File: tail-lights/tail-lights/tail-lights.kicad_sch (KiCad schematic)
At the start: 106 parts, among them IC1 ATMEGA328P-AU, IC2 NCV8402ASTT1G, IC3 NCV8402ASTT1G, IC4 NCV8402ASTT1G, IC5 TPS62160DGKR, J1 Conn_01x01, J2 Conn_01x01, J3 Conn_01x06_Female, J4 Conn_01x04_Female, Y1 X322516MLB4SI

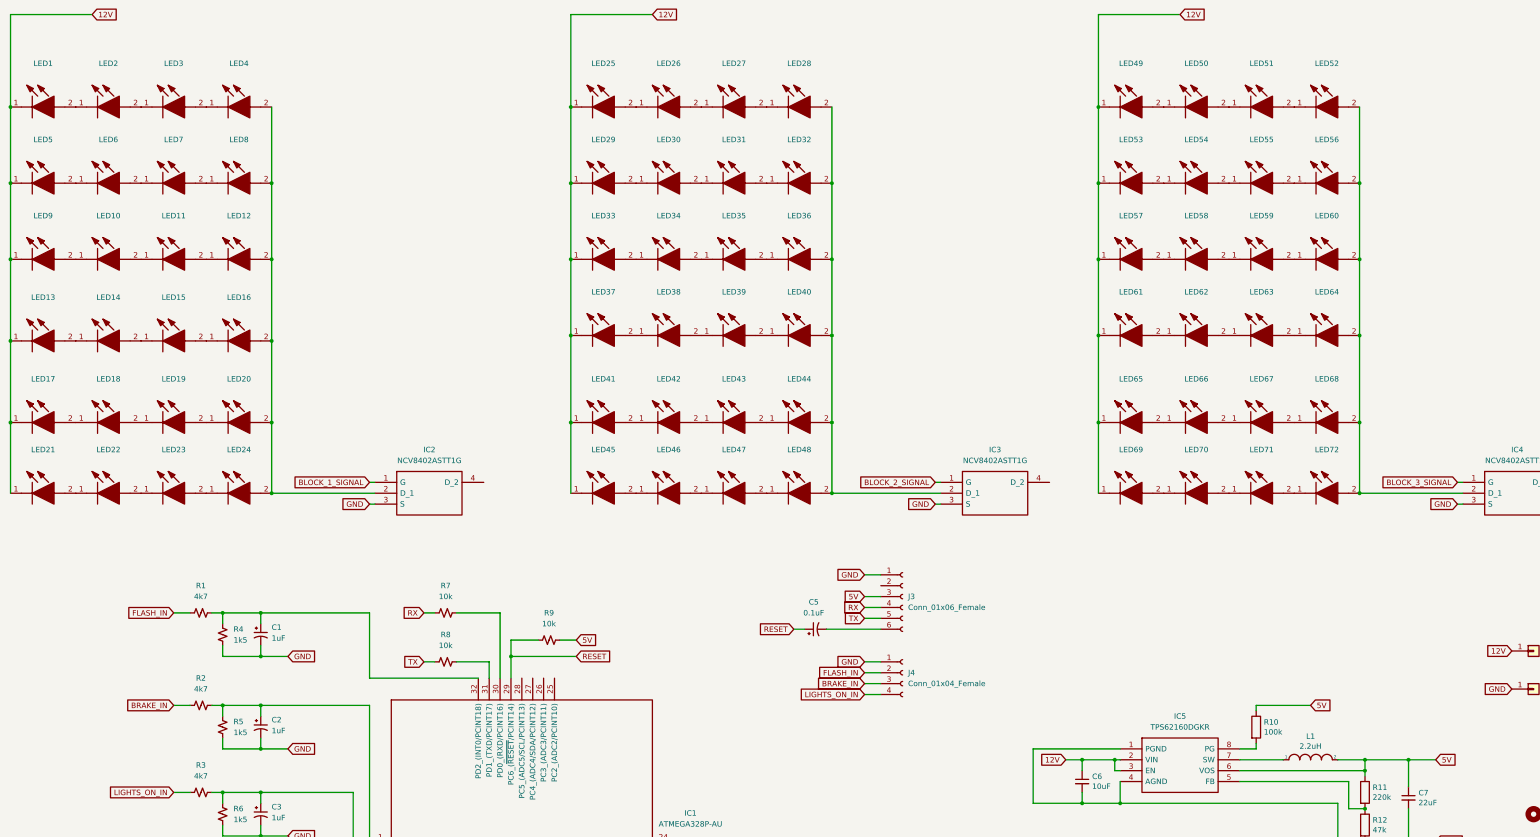
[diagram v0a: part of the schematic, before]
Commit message: Finalise tail-lights. Send off for fab
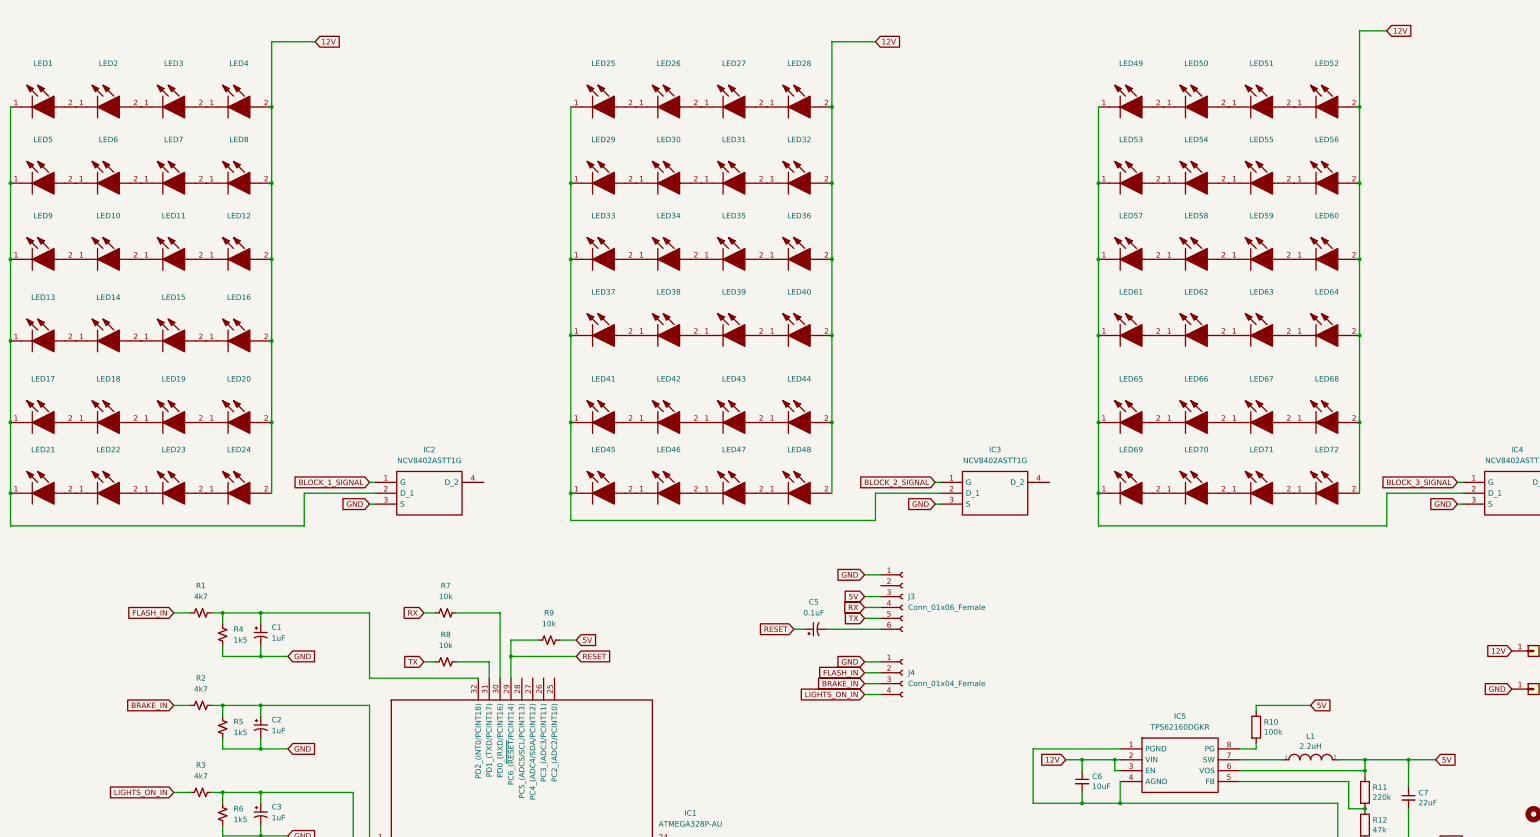
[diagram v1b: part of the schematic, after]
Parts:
- L1: footprint Inductor_SMD:NR6028T220M -> Library:NR6028T220M
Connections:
- net 12V: now also LED12.2, LED16.2, LED20.2, LED24.2, LED28.2, LED32.2, LED36.2, LED4.2, LED40.2, LED44.2, LED48.2, LED52.2, LED56.2, LED60.2, LED64.2, LED68.2, LED72.2, LED8.2; no longer LED1.1, LED13.1, LED17.1, LED21.1, LED25.1, LED29.1, LED33.1, LED37.1, LED41.1, LED45.1, LED49.1, LED5.1, LED53.1, LED57.1, LED61.1, LED65.1, LED69.1, LED9.1
- new net: IC2.2 (D_1), LED1.1, LED13.1, LED17.1, LED21.1, LED5.1, LED9.1
- new net: IC4.2 (D_1), LED49.1, LED53.1, LED57.1, LED61.1, LED65.1, LED69.1
- new net: IC3.2 (D_1), LED25.1, LED29.1, LED33.1, LED37.1, LED41.1, LED45.1

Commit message: Send tail lights v2 for fabrication
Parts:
- removed H1, H2, H3, H4: MountingHole, MountingHole:MountingHole_2.5mm_Pad, symbol Mechanical:MountingHole
- added C8: 0.1uF, Capacitor_SMD:C_0603_1608Metric, symbol Device:C_Polarized_Small_US
- added H1, H2, H3, H5: MountingHole_Pad, MountingHole:MountingHole_2.5mm_Pad, symbol Mechanical:MountingHole_Pad
- added IC6, IC7, IC8: L7812CV, Library:TO255P460X1020X2008-3P, symbol Power_Protection:L7812CV
- added J10, J11, J12, J13, J14, J15, J16, J6, J7, J8, J9: Conn_01x01_Pin, Connector_PinHeader_2.54mm:PinHeader_1x01_P2.54mm_Vertical, symbol Connector:Conn_01x01_Pin
- added J5: Conn_01x06_Female, Connector_PinHeader_2.54mm:PinHeader_1x06_P2.54mm_Vertical, symbol Connector:Conn_01x06_Female
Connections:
- net 12V: now also IC6.1 (INPUT), IC7.1 (INPUT), IC8.1 (INPUT); no longer LED12.2, LED16.2, LED20.2, LED24.2, LED28.2, LED32.2, LED36.2, LED4.2, LED40.2, LED44.2, LED48.2, LED52.2, LED56.2, LED60.2, LED64.2, LED68.2, LED72.2, LED8.2
- net 5V: now also J5.2 (Pin_2)
- net BLOCK_1_SIGNAL: now also IC1.9 ((PCINT21/OC0B/T1)_PD5); no longer IC1.10 ((PCINT22/OC0A/AIN0)_PD6)
- net BLOCK_2_SIGNAL: now also IC1.10 ((PCINT22/OC0A/AIN0)_PD6); no longer IC1.13 ((PCINT1/OC1A)_PB1)
- net BLOCK_3_SIGNAL: now also IC1.13 ((PCINT1/OC1A)_PB1); no longer IC1.15 ((PCINT3/OC2A/MOSI)_PB3)
- net GND: now also H1.1, H2.1, H3.1, H5.1, IC6.2 (GROUND), IC7.2 (GROUND), IC8.2 (GROUND), J5.6 (Pin_6)
- net RESET: now also C8.1
- net at IC1.11 ((PCINT23/AIN1)_PD7): now also J10.1 (Pin_1)
- net at IC1.12 ((PCINT0/CLKO/ICP1)_PB0): now also J11.1 (Pin_1)
- net at IC1.14 ((PCINT2/SS/OC1B)_PB2): now also J12.1 (Pin_1)
- net MISO: now reaches IC1.16 ((PCINT4/MISO)_PB4)
- net MISO: now also J5.1 (Pin_1)
- net SCK: now reaches IC1.17 (PB5_(SCK/PCINT5))
- net SCK: now also J5.3 (Pin_3)
- net at IC1.19 (ADC6): now also J9.1 (Pin_1)
- net at IC1.22 (ADC7): now also J8.1 (Pin_1)
- net at IC1.23 (PC0_(ADC0/PCINT8)): now also J7.1 (Pin_1)
- net at IC1.24 (PC1_(ADC1/PCINT9)): now also J6.1 (Pin_1)
- net at IC1.25 (PC2_(ADC2/PCINT10)): now also J16.1 (Pin_1)
- net at IC1.26 (PC3_(ADC3/PCINT11)): now also J15.1 (Pin_1)
- net at IC1.27 (PC4_(ADC4/SDA/PCINT12)): now also J14.1 (Pin_1)
- net at IC1.28 (PC5_(ADC5/SCL/PCINT13)): now also J13.1 (Pin_1)
- new net: IC8.3 (OUTPUT), LED52.2, LED56.2, LED60.2, LED64.2, LED68.2, LED72.2
- new net: C8.2, J5.5 (Pin_5)
- new net: IC6.3 (OUTPUT), LED12.2, LED16.2, LED20.2, LED24.2, LED4.2, LED8.2
- new net: IC7.3 (OUTPUT), LED28.2, LED32.2, LED36.2, LED40.2, LED44.2, LED48.2
- new net MOSI: IC1.15 ((PCINT3/OC2A/MOSI)_PB3), J5.4 (Pin_4)
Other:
- moved on the sheet: C1, C2, C3, C4, C5, C6, C7, IC1, IC5, J3, J4, L1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
